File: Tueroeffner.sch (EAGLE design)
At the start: 41 parts, among them IC1 NCP1117ST33T3G, IC3 M25PE20, K2 EC2-12TNU, Q1 2N7002CK, Q2 2N7002CK

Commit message: Final RC
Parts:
- added C1: 10µF, eagle-ltspice:CC2012
- C6: value 10µF -> 100nF
- IC1: value NCP1117ST33T3G -> NCV4264-2ST33T3G; device burr-brown:REG1117 -> burr-brown:REG1118
- LED4: value (none) -> RED
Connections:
- net GND: now also C1.2
- net VCC-3.3V: now also C1.1
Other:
- moved on the sheet: C6, IC1, IC3, R3

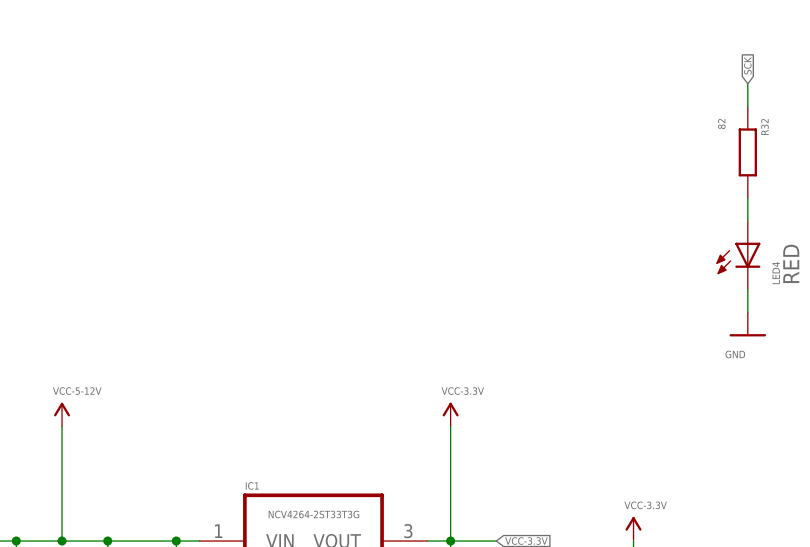
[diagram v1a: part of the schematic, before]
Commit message: Add voltage divider
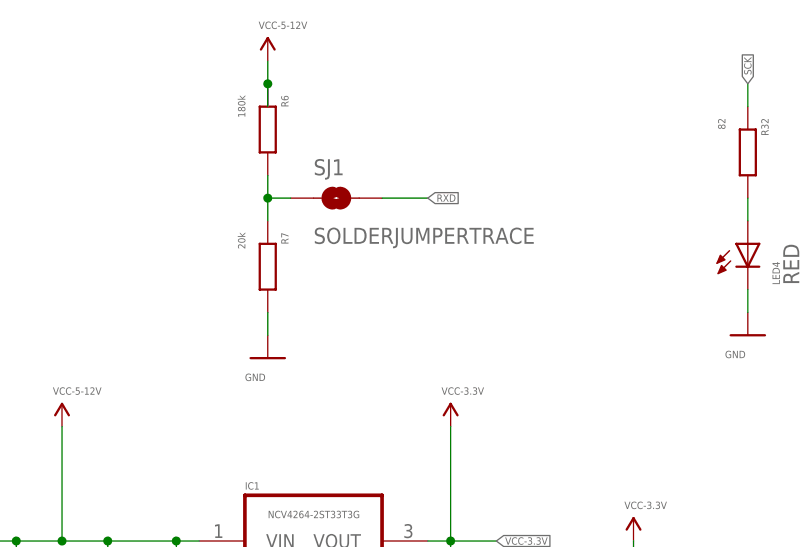
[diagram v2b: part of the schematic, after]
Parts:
- added R6: 180k, resistor:R-EU_M2012
- added R7: 20k, resistor:R-EU_M2012
- added SJ1: SOLDERJUMPERTRACE, SparkFun:SOLDERJUMPERTRACE
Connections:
- new net N$2: R6.2, R7.1, SJ1.1
- net DC_5-12V: now also R6.1
- net GND: now also R7.2
- net RXD: now also SJ1.2
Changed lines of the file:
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@@
 <part name="SK" library="testpad" deviceset="TP" device="TP14R" value="TPTP14R"/>
 <part name="C1" library="eagle-ltspice" deviceset="C" device="C2012" value="10µF"/>
+<part name="R6" library="resistor" deviceset="R-EU_" device="M2012" value="180k"/>
+<part name="R7" library="resistor" deviceset="R-EU_" device="M2012" value="20k"/>
+<part name="5-12V3" library="SparkFun-Aesthetics" deviceset="VCC" device="" value="VCC-5-12V"/>
+<part name="GND8" library="SparkFun-Aesthetics" deviceset="GND" device=""/>
+<part name="SJ1" library="SparkFun" deviceset="SOLDERJUMPER" device="TRACE"/>
 </parts>
 <sheets>
@@
 <attribute name="VALUE" x="169.164" y="23.241" size="0.8128" layer="96"/>
 </instance>
+<instance part="R6" gate="G$1" x="66.04" y="83.82" smashed="yes" rot="R270">
+<attribute name="NAME" x="67.5386" y="87.63" size="0.8128" layer="95" rot="R270"/>
+<attribute name="VALUE" x="62.738" y="87.63" size="0.8128" layer="96" rot="R270"/>
+</instance>
+<instance part="R7" gate="G$1" x="66.04" y="68.58" smashed="yes" rot="R270">
+<attribute name="NAME" x="67.5386" y="72.39" size="0.8128" layer="95" rot="R270"/>
+<attribute name="VALUE" x="62.738" y="72.39" size="0.8128" layer="96" rot="R270"/>
+</instance>
+<instance part="5-12V3" gate="G$1" x="66.04" y="91.44" smashed="yes">
+<attribute name="VALUE" x="65.024" y="94.996" size="0.8128" layer="96"/>
+</instance>
+<instance part="GND8" gate="1" x="66.04" y="58.42" smashed="yes">
+<attribute name="VALUE" x="63.5" y="55.88" size="0.8128" layer="96"/>
+</instance>
+<instance part="SJ1" gate="1" x="73.66" y="76.2"/>
 </instances>
 <busses>
@@
 <wire x1="320.04" y1="43.18" x2="320.04" y2="40.64" width="0.1524" layer="91"/>
 </segment>
+<segment>
+<pinref part="R7" gate="G$1" pin="2"/>
+<pinref part="GND8" gate="1" pin="GND"/>
+<wire x1="66.04" y1="63.5" x2="66.04" y2="60.96" width="0.1524" layer="91"/>
+</segment>
 </net>
 <net name="DC_5-12V" class="0">
@@
 <junction x="304.8" y="43.18"/>
 </segment>
+<segment>
+<wire x1="66.04" y1="91.44" x2="66.04" y2="88.9" width="0.1524" layer="91"/>
+<pinref part="5-12V3" gate="G$1" pin="VCC"/>
+<pinref part="R6" gate="G$1" pin="1"/>
+<wire x1="66.04" y1="88.9" x2="66.04" y2="86.36" width="0.1524" layer="91"/>
+<junction x="66.04" y="88.9"/>
+</segment>
 </net>
 <net name="VCC-3.3V" class="0">
@@
 <pinref part="RX" gate="G$1" pin="TP"/>
 <wire x1="154.94" y1="78.74" x2="149.86" y2="78.74" width="0.1524" layer="91"/>
+</segment>
+<segment>
+<label x="83.82" y="76.2" size="0.8128" layer="95" xref="yes"/>
+<pinref part="SJ1" gate="1" pin="2"/>
+<wire x1="78.74" y1="76.2" x2="83.82" y2="76.2" width="0.1524" layer="91"/>
 </segment>
 </net>
@@
 </segment>
 </net>
+<net name="N$2" class="0">
+<segment>
+<pinref part="R7" gate="G$1" pin="1"/>
+<pinref part="SJ1" gate="1" pin="1"/>
+<pinref part="R6" gate="G$1" pin="2"/>
+<wire x1="66.04" y1="78.74" x2="66.04" y2="76.2" width="0.1524" layer="91"/>
+<wire x1="66.04" y1="76.2" x2="68.58" y2="76.2" width="0.1524" layer="91"/>
+<junction x="66.04" y="76.2"/>
+<wire x1="66.04" y1="76.2" x2="66.04" y2="73.66" width="0.1524" layer="91"/>
+</segment>
+</net>

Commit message: BOM
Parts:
- C1, C3: value 10µF -> 100nF
- C5: value 0.1µF -> 100nF
- D1: value SMAJ20A -> SMAJ24A
- IC1: value NCV4264-2ST33T3G -> IFX25001MEV33HTSA1
- R32: value 82 -> 330
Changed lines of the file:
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@@
 <part name="GND14" library="SparkFun-Aesthetics" deviceset="GND" device=""/>
 <part name="C2" library="rcl" deviceset="C-EU" device="C0805" value="10µF"/>
-<part name="D1" library="SparkFun-DiscreteSemi" deviceset="TVS" device="SMA" value="SMAJ20A"/>
-<part name="IC1" library="burr-brown" deviceset="REG1118" device="" value="NCV4264-2ST33T3G"/>
+<part name="D1" library="SparkFun-DiscreteSemi" deviceset="TVS" device="SMA" value="SMAJ24A"/>
+<part name="IC1" library="burr-brown" deviceset="REG1118" device="" value="IFX25001MEV33HTSA1"/>
 <part name="JP1" library="SparkFun-Connectors" deviceset="M01" device="PTH" value="Z-Antenna"/>
 <part name="GND1" library="SparkFun-Aesthetics" deviceset="GND" device=""/>
@@
 <part name="C4" library="eagle-ltspice" deviceset="C" device="C2012" value="15pF"/>
 <part name="U$5" library="ZM5202" deviceset="ZM5202" device="ZM5202_STERN" value="ZM5202"/>
-<part name="C3" library="eagle-ltspice" deviceset="C" device="C2012" value="10µF"/>
+<part name="C3" library="eagle-ltspice" deviceset="C" device="C2012" value="100nF"/>
 <part name="C6" library="eagle-ltspice" deviceset="C" device="C2012" value="100nF"/>
 <part name="GND16" library="SparkFun-Aesthetics" deviceset="GND" device=""/>
@@
 <part name="GND18" library="SparkFun-Aesthetics" deviceset="GND" device=""/>
 <part name="LED4" library="adafruit" deviceset="LED" device="CHIP-LED0805" value="RED"/>
-<part name="R32" library="resistor" deviceset="R-EU_" device="M2012" value="82"/>
+<part name="R32" library="resistor" deviceset="R-EU_" device="M2012" value="330"/>
 <part name="GND19" library="SparkFun-Aesthetics" deviceset="GND" device=""/>
 <part name="R1" library="rcl" deviceset="R-EU_" device="M0805" value="4.7K"/>
-<part name="C5" library="rcl" deviceset="C-EU" device="C0805" value="0.1µF"/>
+<part name="C5" library="rcl" deviceset="C-EU" device="C0805" value="100nF"/>
 <part name="GND2" library="supply1" deviceset="GND" device=""/>
 <part name="P+1" library="supply1" deviceset="VCC" device="" value="VCC-3.3V"/>
@@
 <part name="RS" library="testpad" deviceset="TP" device="TP14R" value="TPTP14R"/>
 <part name="SK" library="testpad" deviceset="TP" device="TP14R" value="TPTP14R"/>
-<part name="C1" library="eagle-ltspice" deviceset="C" device="C2012" value="10µF"/>
+<part name="C1" library="eagle-ltspice" deviceset="C" device="C2012" value="100nF"/>
 <part name="R6" library="resistor" deviceset="R-EU_" device="M2012" value="180k"/>
 <part name="R7" library="resistor" deviceset="R-EU_" device="M2012" value="20k"/>

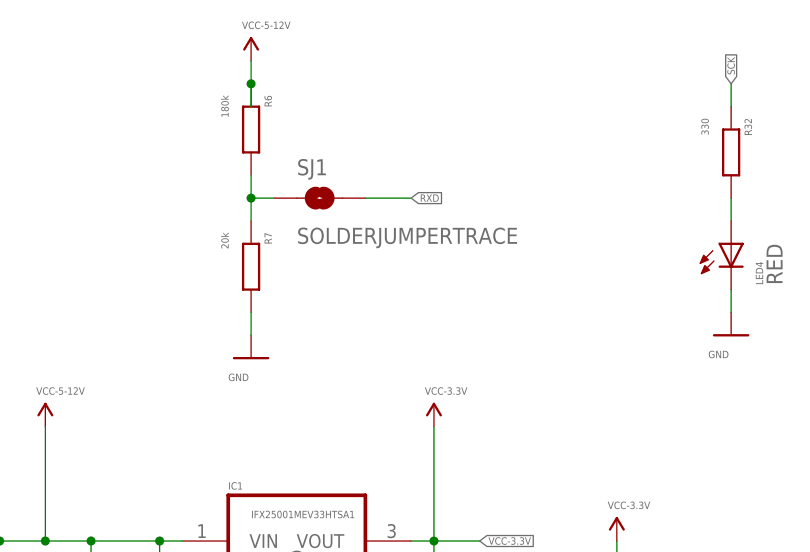
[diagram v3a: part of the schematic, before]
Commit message: Voltage Divider Cap
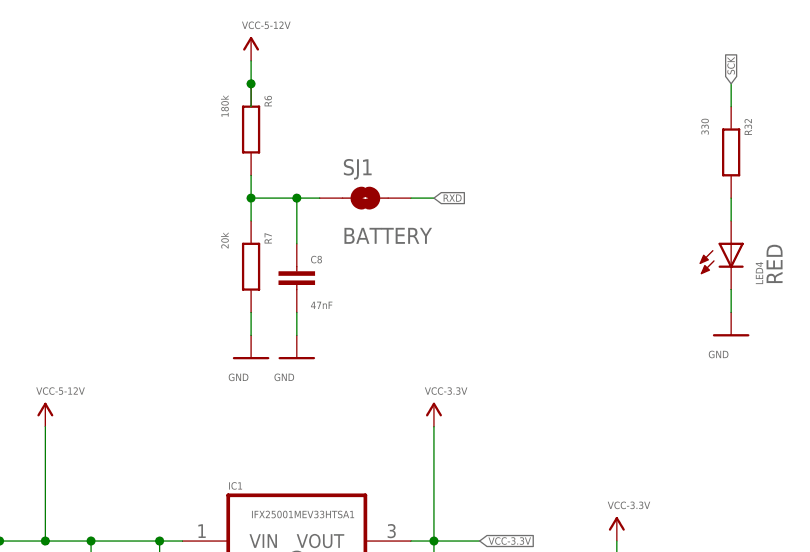
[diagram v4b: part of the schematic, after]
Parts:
- added C8: 47nF, eagle-ltspice:CC2012
- SJ1: value SOLDERJUMPERTRACE -> BATTERY
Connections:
- net GND: now also C8.2
- net N$2: now also C8.1
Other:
- moved on the sheet: SJ1
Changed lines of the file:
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@@
 <part name="5-12V3" library="SparkFun-Aesthetics" deviceset="VCC" device="" value="VCC-5-12V"/>
 <part name="GND8" library="SparkFun-Aesthetics" deviceset="GND" device=""/>
-<part name="SJ1" library="SparkFun" deviceset="SOLDERJUMPER" device="TRACE"/>
+<part name="SJ1" library="SparkFun" deviceset="SOLDERJUMPER" device="TRACE" value="BATTERY"/>
+<part name="C8" library="eagle-ltspice" deviceset="C" device="C2012" value="47nF"/>
+<part name="GND9" library="SparkFun-Aesthetics" deviceset="GND" device=""/>
 </parts>
 <sheets>
@@
 <attribute name="VALUE" x="63.5" y="55.88" size="0.8128" layer="96"/>
 </instance>
-<instance part="SJ1" gate="1" x="73.66" y="76.2"/>
+<instance part="SJ1" gate="1" x="78.74" y="76.2"/>
+<instance part="C8" gate="G$1" x="71.12" y="68.58" smashed="yes">
+<attribute name="NAME" x="72.644" y="68.961" size="0.8128" layer="95"/>
+<attribute name="VALUE" x="72.644" y="63.881" size="0.8128" layer="96"/>
+</instance>
+<instance part="GND9" gate="1" x="71.12" y="58.42" smashed="yes">
+<attribute name="VALUE" x="68.58" y="55.88" size="0.8128" layer="96"/>
+</instance>
 </instances>
 <busses>
@@
 <wire x1="66.04" y1="63.5" x2="66.04" y2="60.96" width="0.1524" layer="91"/>
 </segment>
+<segment>
+<pinref part="GND9" gate="1" pin="GND"/>
+<pinref part="C8" gate="G$1" pin="2"/>
+<wire x1="71.12" y1="60.96" x2="71.12" y2="63.5" width="0.1524" layer="91"/>
+</segment>
 </net>
 <net name="DC_5-12V" class="0">
@@
 </segment>
 <segment>
-<label x="83.82" y="76.2" size="0.8128" layer="95" xref="yes"/>
+<label x="86.36" y="76.2" size="0.8128" layer="95" xref="yes"/>
 <pinref part="SJ1" gate="1" pin="2"/>
-<wire x1="78.74" y1="76.2" x2="83.82" y2="76.2" width="0.1524" layer="91"/>
+<wire x1="83.82" y1="76.2" x2="86.36" y2="76.2" width="0.1524" layer="91"/>
 </segment>
 </net>
@@
 <pinref part="R6" gate="G$1" pin="2"/>
 <wire x1="66.04" y1="78.74" x2="66.04" y2="76.2" width="0.1524" layer="91"/>
-<wire x1="66.04" y1="76.2" x2="68.58" y2="76.2" width="0.1524" layer="91"/>
+<wire x1="66.04" y1="76.2" x2="71.12" y2="76.2" width="0.1524" layer="91"/>
 <junction x="66.04" y="76.2"/>
+<wire x1="71.12" y1="76.2" x2="73.66" y2="76.2" width="0.1524" layer="91"/>
 <wire x1="66.04" y1="76.2" x2="66.04" y2="73.66" width="0.1524" layer="91"/>
-</segment>
-</net>
+<pinref part="C8" gate="G$1" pin="1"/>
+<wire x1="71.12" y1="71.12" x2="71.12" y2="76.2" width="0.1524" layer="91"/>
+<junction x="71.12" y="76.2"/>
+</segment>
+</net>
